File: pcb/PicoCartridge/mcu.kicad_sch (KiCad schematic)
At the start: 1 part, among them U1 RP2350B-QFN80

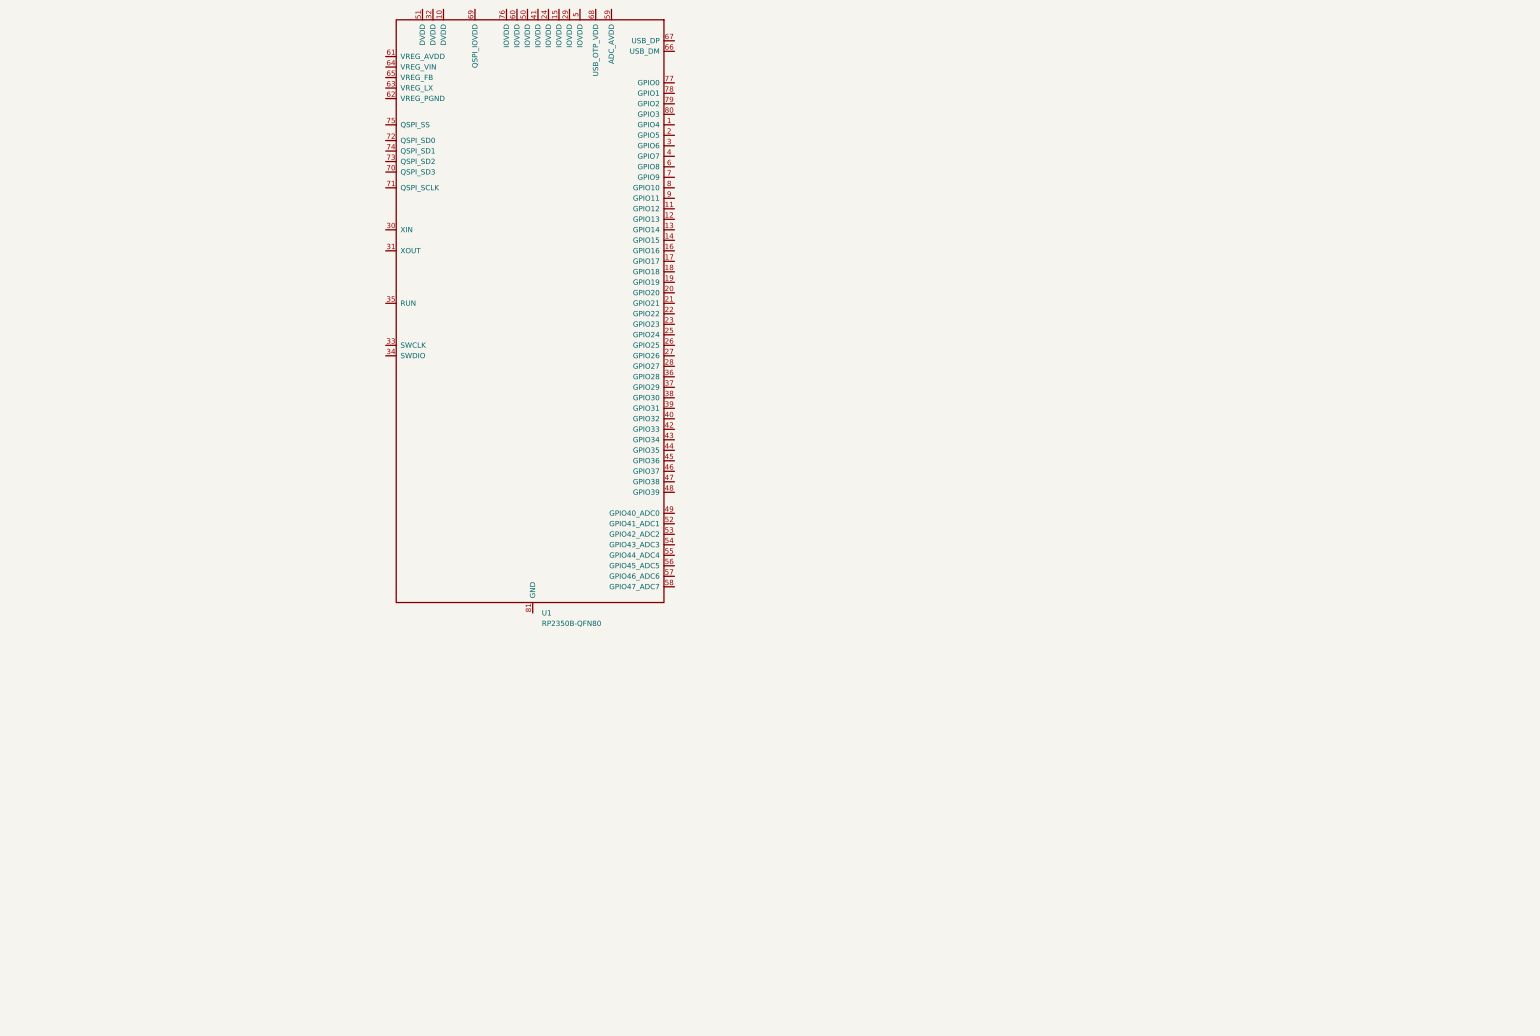
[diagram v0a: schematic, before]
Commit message: Added RP2350 circuitry
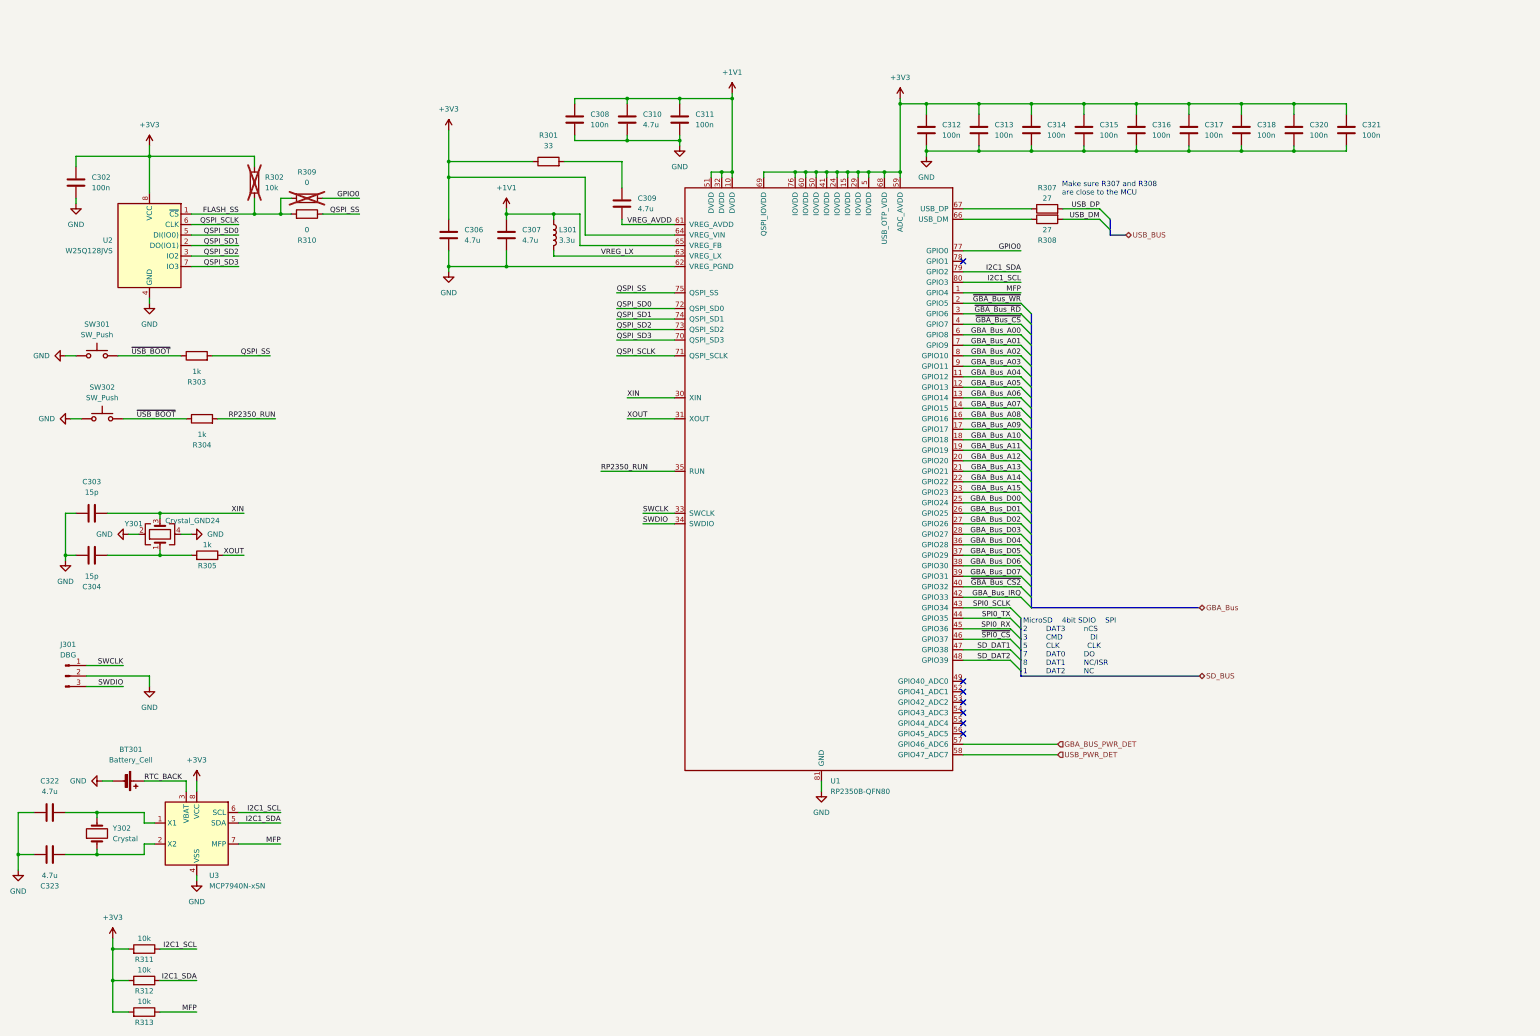
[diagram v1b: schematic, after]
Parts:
- added BT301: Battery_Cell, symbol Device:Battery_Cell
- added C302, C308, C311, C312, C313, C314, C315, C316, C317, C318, C320, C321: 100n, Capacitor_SMD:C_0402_1005Metric, symbol Device:C
- added C303, C304: 15p, Capacitor_SMD:C_0402_1005Metric, symbol Device:C
- added C306, C307, C309, C310, C322, C323: 4.7u, Capacitor_SMD:C_0402_1005Metric, symbol Device:C
- added J301: DBG, Connector_PinHeader_1.27mm:PinHeader_1x03_P1.27mm_Vertical, symbol Connector:Conn_01x03_Pin
- added L301: 3.3u, symbol Device:L
- added R301: 33, Resistor_SMD:R_0402_1005Metric, symbol Device:R
- added R302, R311, R312, R313: 10k, Resistor_SMD:R_0402_1005Metric, symbol Device:R
- added R303, R304, R305: 1k, Resistor_SMD:R_0402_1005Metric, symbol Device:R
- added R307, R308: 27, Resistor_SMD:R_0402_1005Metric, symbol Device:R
- added R309, R310: 0, Resistor_SMD:R_0402_1005Metric, symbol Device:R
- added SW301, SW302: SW_Push, symbol Switch:SW_Push
- added U2: W25Q128JVS, Package_SO:SOIC-8_5.23x5.23mm_P1.27mm, symbol Memory_Flash:W25Q128JVS
- added U3: MCP7940N-xSN, Package_SO:SOIC-8_3.9x4.9mm_P1.27mm, symbol Timer_RTC:MCP7940N-xSN
- added Y301: Crystal_GND24, symbol Device:Crystal_GND24
- added Y302: Crystal, symbol Device:Crystal
- U1: footprint (none) -> RP2350_KiCad:RP2350B_QFN-80_EP_10.573x10.573_Pitch0.4mm
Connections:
- net MFP: now reaches U1.1 (GPIO4)
- net MFP: now also R313.1, U3.7 (MFP)
- net +1V1: now reaches U1.10 (DVDD)
- net +1V1: now also U1.32 (DVDD), U1.51 (DVDD), U1.65 (VREG_FB), C307.1, C308.1, C310.1, C311.1, L301.1
- net GBA_Bus_A04: now reaches U1.11 (GPIO12)
- net GBA_Bus_A05: now reaches U1.12 (GPIO13)
- net GBA_Bus_A06: now reaches U1.13 (GPIO14)
- net GBA_Bus_A07: now reaches U1.14 (GPIO15)
- net +3V3: now reaches U1.15 (IOVDD)
- net +3V3: now also U1.24 (IOVDD), U1.29 (IOVDD), U1.41 (IOVDD), U1.5 (IOVDD), U1.50 (IOVDD), U1.59 (ADC_AVDD), U1.60 (IOVDD), U1.64 (VREG_VIN), U1.68 (USB_OTP_VDD), U1.69 (QSPI_IOVDD), U1.76 (IOVDD), C302.1, C306.1, C312.1, C313.1, C314.1, C315.1, C316.1, C317.1, C318.1, C320.1, C321.1, R301.1, R302.1, R311.2, R312.2, R313.2, U2.8 (VCC), U3.8 (VCC)
- net GBA_Bus_A08: now reaches U1.16 (GPIO16)
- net GBA_Bus_A09: now reaches U1.17 (GPIO17)
- net GBA_Bus_A10: now reaches U1.18 (GPIO18)
- net GBA_Bus_A11: now reaches U1.19 (GPIO19)
- net ~{GBA_Bus_WR}: now reaches U1.2 (GPIO5)
- net GBA_Bus_A12: now reaches U1.20 (GPIO20)
- net GBA_Bus_A13: now reaches U1.21 (GPIO21)
- net GBA_Bus_A14: now reaches U1.22 (GPIO22)
- net GBA_Bus_A15: now reaches U1.23 (GPIO23)
- net GBA_Bus_D00: now reaches U1.25 (GPIO24)
- net GBA_Bus_D01: now reaches U1.26 (GPIO25)
- net GBA_Bus_D02: now reaches U1.27 (GPIO26)
- net GBA_Bus_D03: now reaches U1.28 (GPIO27)
- net ~{GBA_Bus_RD}: now reaches U1.3 (GPIO6)
- net XIN: now reaches U1.30 (XIN)
- net XIN: now also C303.2, Y301.3
- net XOUT: now reaches U1.31 (XOUT)
- net XOUT: now also R305.1
- net SWCLK: now reaches U1.33 (SWCLK)
- net SWCLK: now also J301.1 (Pin_1)
- net SWDIO: now reaches U1.34 (SWDIO)
- net SWDIO: now also J301.3 (Pin_3)
- net RP2350_RUN: now reaches U1.35 (RUN)
- net RP2350_RUN: now also R304.2
- net GBA_Bus_D04: now reaches U1.36 (GPIO28)
- net GBA_Bus_D05: now reaches U1.37 (GPIO29)
- net GBA_Bus_D06: now reaches U1.38 (GPIO30)
- net GBA_Bus_D07: now reaches U1.39 (GPIO31)
- net ~{GBA_Bus_CS}: now reaches U1.4 (GPIO7)
- net ~{GBA_Bus_CS2}: now reaches U1.40 (GPIO32)
- net GBA_Bus_IRQ: now reaches U1.42 (GPIO33)
- net SPI0_SCLK: now reaches U1.43 (GPIO34)
- net SPI0_TX: now reaches U1.44 (GPIO35)
- net SPI0_RX: now reaches U1.45 (GPIO36)
- net ~{SPI0_CS}: now reaches U1.46 (GPIO37)
- net SD_DAT1: now reaches U1.47 (GPIO38)
- net SD_DAT2: now reaches U1.48 (GPIO39)
- net GBA_BUS_PWR_DET: now reaches U1.57 (GPIO46_ADC6)
- net USB_PWR_DET: now reaches U1.58 (GPIO47_ADC7)
- net GBA_Bus_A00: now reaches U1.6 (GPIO8)
- net VREG_AVDD: now reaches U1.61 (VREG_AVDD)
- net VREG_AVDD: now also C309.2
- net GND: now reaches U1.62 (VREG_PGND)
- net GND: now also U1.81 (GND), BT301.2 (-), C302.2, C303.1, C304.1, C306.2, C307.2, C308.2, C310.2, C311.2, C312.2, C313.2, C314.2, C315.2, C316.2, C317.2, C318.2, C320.2, C321.2, C322.1, C323.1, J301.2 (Pin_2), SW301.2, SW302.2, U2.4 (GND), U3.4 (VSS), Y301.2, Y301.4
- net VREG_LX: now reaches U1.63 (VREG_LX)
- net VREG_LX: now also L301.2
- net at U1.66 (USB_DM): now also R308.1
- net at U1.67 (USB_DP): now also R307.1
- net GBA_Bus_A01: now reaches U1.7 (GPIO9)
- net QSPI_SD3: now reaches U1.70 (QSPI_SD3)
- net QSPI_SD3: now also U2.7 (IO3)
- net QSPI_SCLK: now reaches U1.71 (QSPI_SCLK)
- net QSPI_SCLK: now also U2.6 (CLK)
- net QSPI_SD0: now reaches U1.72 (QSPI_SD0)
- net QSPI_SD0: now also U2.5 (DI(IO0))
- net QSPI_SD2: now reaches U1.73 (QSPI_SD2)
- net QSPI_SD2: now also U2.3 (IO2)
- net QSPI_SD1: now reaches U1.74 (QSPI_SD1)
- net QSPI_SD1: now also U2.2 (DO(IO1))
- net QSPI_SS: now reaches U1.75 (QSPI_SS)
- net QSPI_SS: now also R303.2, R310.1
- net GPIO0: now reaches U1.77 (GPIO0)
- net GPIO0: now also R309.1
- net I2C1_SDA: now reaches U1.79 (GPIO2)
- net I2C1_SDA: now also R312.1, U3.5 (SDA)
- net GBA_Bus_A02: now reaches U1.8 (GPIO10)
- net I2C1_SCL: now reaches U1.80 (GPIO3)
- net I2C1_SCL: now also R311.1, U3.6 (SCL)
- net GBA_Bus_A03: now reaches U1.9 (GPIO11)
- new net: C323.2, U3.2 (X2), Y302.1
- new net: C322.2, U3.1 (X1), Y302.2
- new net: C309.1, R301.2
- new net: C304.2, R305.2, Y301.1
- new net FLASH_SS: R302.2, R309.2, R310.2, U2.1 (~{CS})
- new net RTC_BACK: BT301.1 (+), U3.3 (VBAT)
- new net USB_DM: R308.2
- new net USB_DP: R307.2
- new net ~{USB_BOOT}: R303.1, R304.1, SW301.1, SW302.1
- no-connect marks 0 -> 7
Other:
- note added: "Make sure R307 and R308 are close to the MCU"
- note added: "MicroSD 4bit SDIO SPI 2 DAT3 nCS 3 CMD DI 5 CLK CLK 7 DAT0 DO 8 DAT1 NC/ISR 1 DAT2 NC"
- moved on the sheet: U1

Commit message: Added base pcb layout
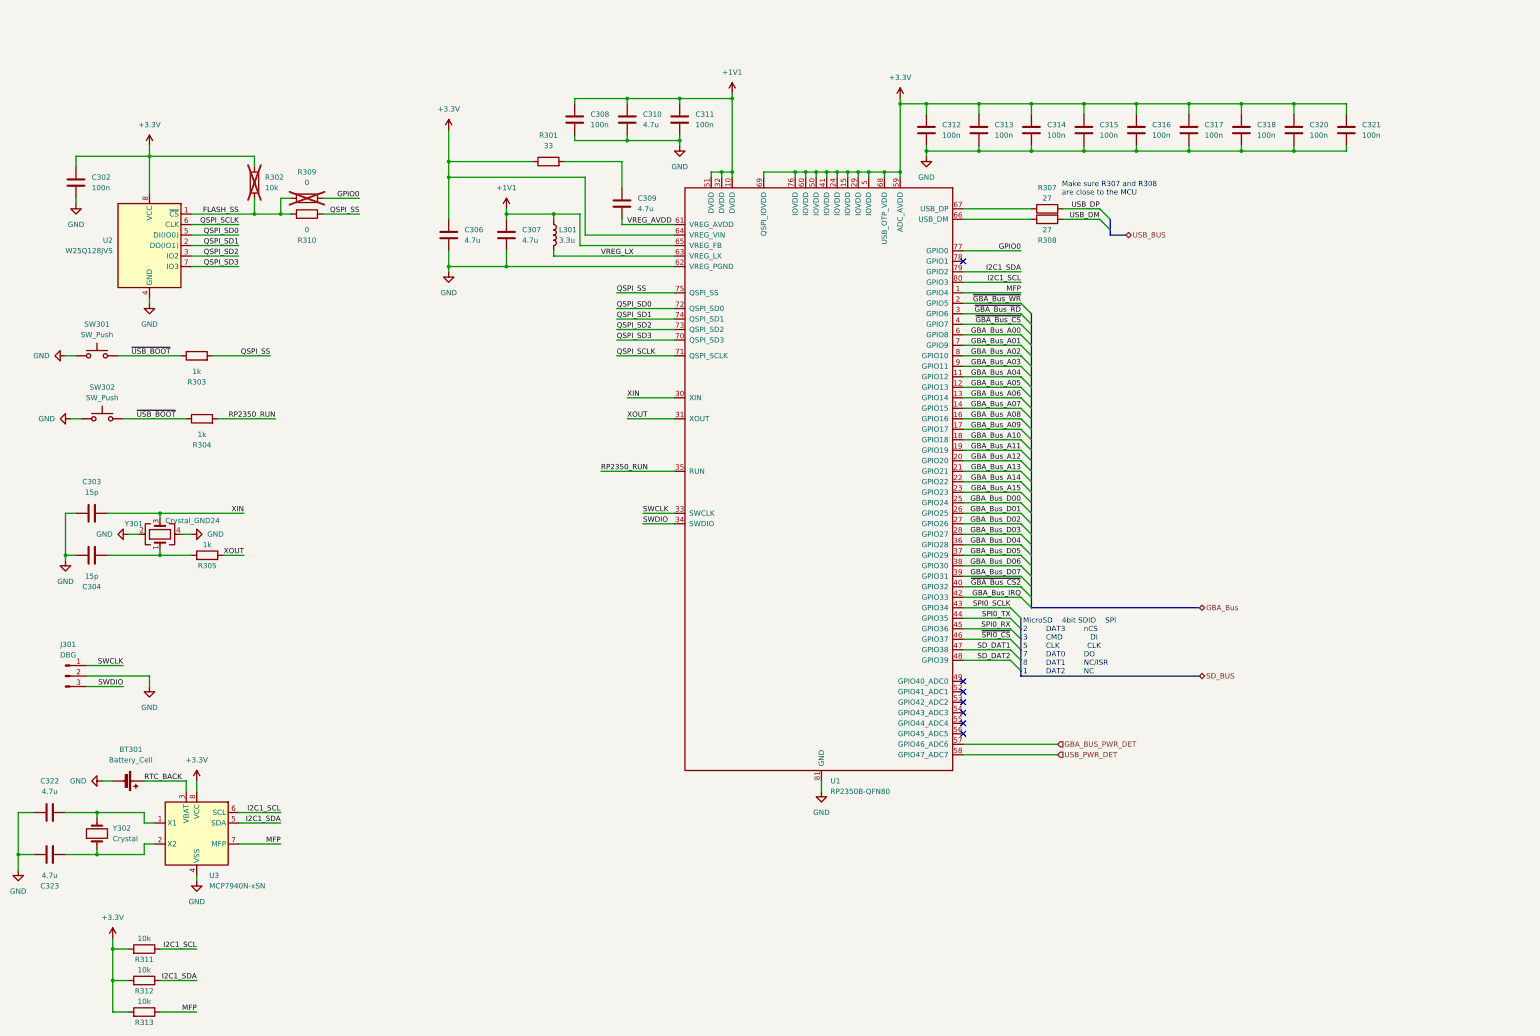
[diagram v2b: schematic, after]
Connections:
- net +3V3 renamed +3.3V

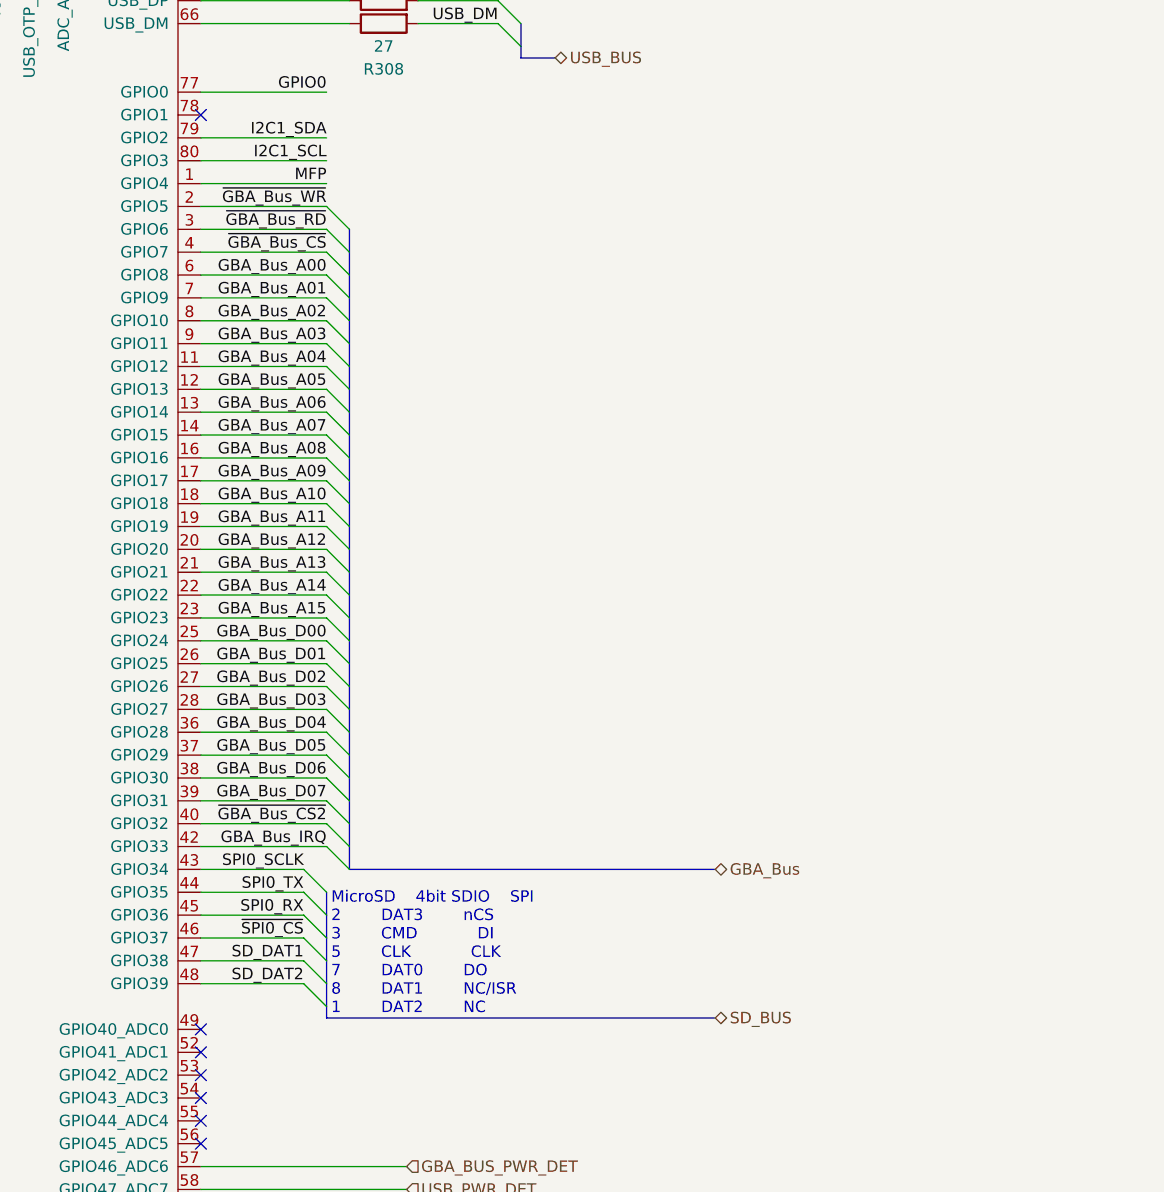
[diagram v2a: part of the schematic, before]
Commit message: Fixed connection between MCU and SD card
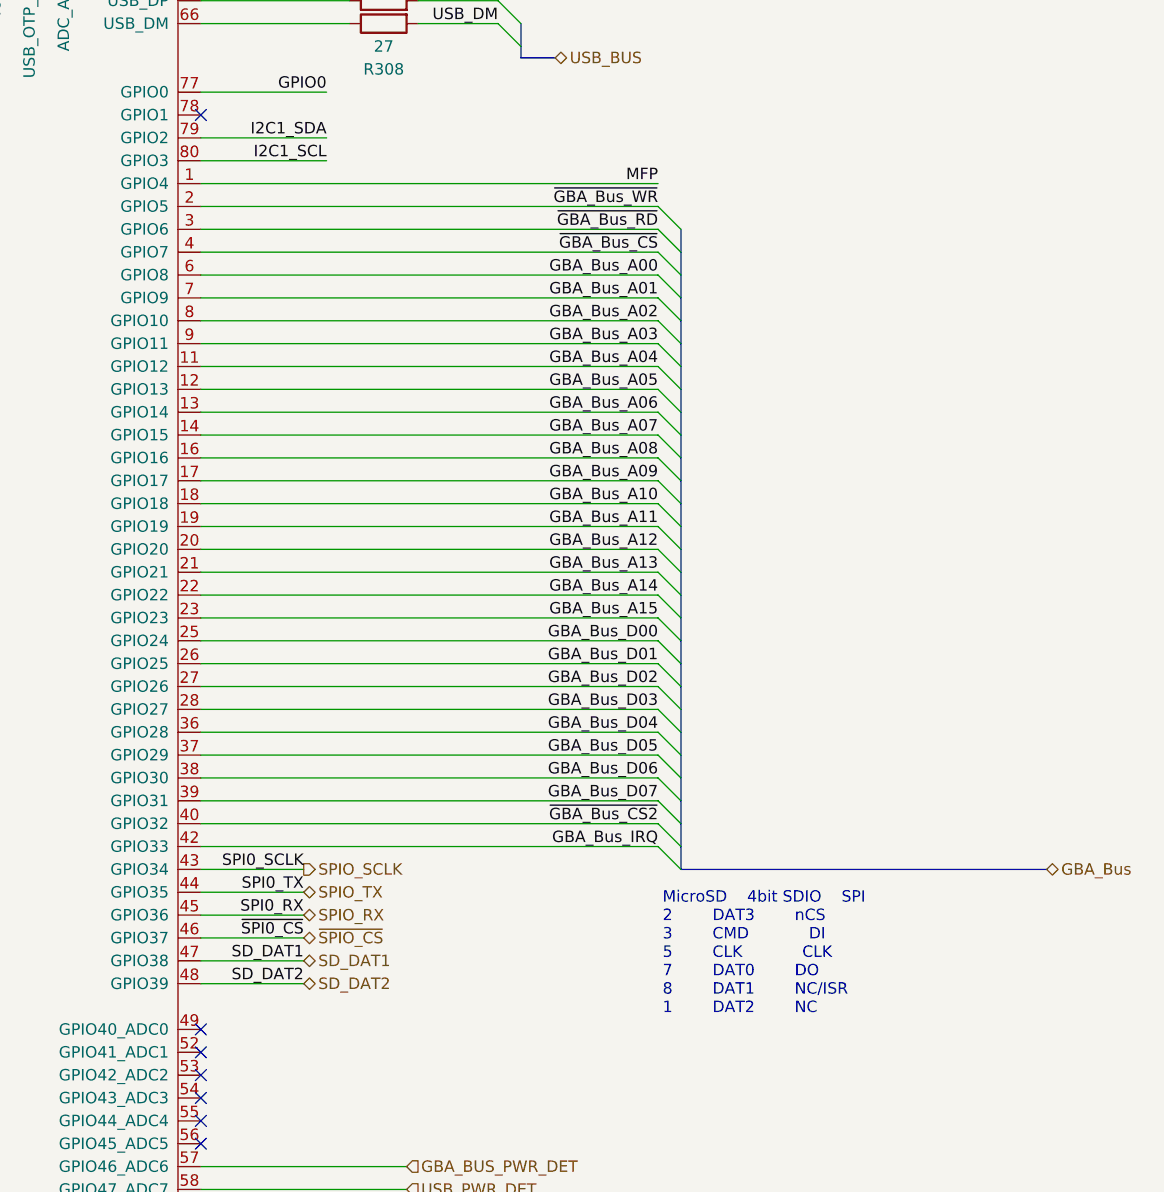
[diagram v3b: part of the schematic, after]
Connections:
- net SPI0_RX renamed SPIO_RX
- net SPI0_SCLK renamed SPIO_SCLK
- net SPI0_TX renamed SPIO_TX
- net ~{SPI0_CS} renamed ~{SPIO_CS}
